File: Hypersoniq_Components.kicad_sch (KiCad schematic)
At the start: 33 parts, among them J1 Conn_01x10_Pin, J2 Conn_01x10_Pin, J3 Conn_01x10_Pin, J4 Eurorack_10_pin_power, U1 TL074, U6 TL072

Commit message: v1.0 Design sent for manufacture
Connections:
- net +12V: now also U6.8 (V+); no longer U6.4 (V-)
- net -12V: now also J3.5 (Pin_5), U6.4 (V-); no longer U6.8 (V+)
- net GND: no longer J3.5 (Pin_5)
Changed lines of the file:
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@@
   (junction (at 35.56 154.94) (diameter 0) (color 0 0 0 0)
   )
+  (junction (at 265.43 138.43) (diameter 0) (color 0 0 0 0)
+  )
   (junction (at 62.23 101.6) (diameter 1.016) (color 0 0 0 0)
   )
@@
   )
   (wire (pts (xy 58.42 171.45) (xy 58.42 172.72))
+    (stroke (width 0) (type default))
+  )
+  (wire (pts (xy 265.43 138.43) (xy 265.43 140.97))
     (stroke (width 0) (type default))
   )
@@
         (path "/5bf2ff82-d6ae-4b65-8172-8e3e49f5daf5"
           (reference "D2") (unit 1)
+        )
+      )
+    )
+  )
+  (symbol (lib_id "power:-12V") (at 265.43 133.35 270) (unit 1)
+    (in_bom yes) (on_board yes) (dnp no)
+    (property "Reference" "#PWR09" (at 267.97 133.35 0)
+      (effects (font (size 1.27 1.27)) hide)
+    )
+    (property "Value" "-12V" (at 267.97 132.08 90)
+      (effects (font (size 1.27 1.27)) (justify left))
+    )
+    (property "Footprint" "" (at 265.43 133.35 0)
+      (effects (font (size 1.27 1.27)) hide)
+    )
+    (property "Datasheet" "" (at 265.43 133.35 0)
+      (effects (font (size 1.27 1.27)) hide)
+    )
+    (pin "1")
+    (instances
+      (project "Hypersoniq_Components"
+        (path "/3008c47a-0b70-48ce-87af-10c40a725fcd"
+          (reference "#PWR09") (unit 1)
+        )
+      )
+      (project "Quilter_Components"
+        (path "/5bf2ff82-d6ae-4b65-8172-8e3e49f5daf5"
+          (reference "#PWR04") (unit 1)
         )
       )
@@
     )
   )
-  (symbol (lib_id "power:GND") (at 265.43 133.35 90) (unit 1)
-    (in_bom yes) (on_board yes) (dnp no)
-    (property "Reference" "#PWR09" (at 271.78 133.35 0)
-      (effects (font (size 1.27 1.27)) hide)
-    )
-    (property "Value" "GND" (at 268.605 132.715 90)
-      (effects (font (size 1.27 1.27)) (justify right))
-    )
-    (property "Footprint" "" (at 265.43 133.35 0)
-      (effects (font (size 1.27 1.27)) hide)
-    )
-    (property "Datasheet" "" (at 265.43 133.35 0)
-      (effects (font (size 1.27 1.27)) hide)
-    )
-    (pin "1")
-    (instances
-      (project "Hypersoniq_Components"
-        (path "/3008c47a-0b70-48ce-87af-10c40a725fcd"
-          (reference "#PWR09") (unit 1)
-        )
-      )
-      (project "Quilter_Components"
-        (path "/5bf2ff82-d6ae-4b65-8172-8e3e49f5daf5"
-          (reference "#PWR0112") (unit 1)
-        )
-      )
-    )
-  )
   (symbol (lib_id "power:GND") (at 143.51 152.4 270) (unit 1)
     (in_bom yes) (on_board yes) (dnp no)
@@
       (effects (font (size 1.27 1.27)) hide)
     )
-    (property "Value" "GND" (at 268.605 137.795 90)
+    (property "Value" "GND" (at 269.24 138.43 90)
       (effects (font (size 1.27 1.27)) (justify right))
     )
@@
     )
   )
-  (symbol (lib_id "Amplifier_Operational:TL072") (at 106.68 161.29 0) (mirror x) (unit 3)
-    (in_bom yes) (on_board yes) (dnp no)
-    (property "Reference" "U6" (at 109.22 160.02 0)
+  (symbol (lib_id "Amplifier_Operational:TL072") (at 101.6 161.29 0) (mirror y) (unit 3)
+    (in_bom yes) (on_board yes) (dnp no) (fields_autoplaced)
+    (property "Reference" "U6" (at 105.41 160.02 0)
       (effects (font (size 1.27 1.27)) (justify right))
     )
-    (property "Value" "TL072" (at 111.76 162.56 0)
+    (property "Value" "TL072" (at 105.41 162.56 0)
       (effects (font (size 1.27 1.27)) (justify right))
     )
-    (property "Footprint" "Package_SO:SO-8_3.9x4.9mm_P1.27mm" (at 106.68 161.29 0)
-      (effects (font (size 1.27 1.27)) hide)
-    )
-    (property "Datasheet" "http://www.ti.com/lit/ds/symlink/tl071.pdf" (at 106.68 161.29 0)
+    (property "Footprint" "Package_SO:SO-8_3.9x4.9mm_P1.27mm" (at 101.6 161.29 0)
+      (effects (font (size 1.27 1.27)) hide)
+    )
+    (property "Datasheet" "http://www.ti.com/lit/ds/symlink/tl071.pdf" (at 101.6 161.29 0)
       (effects (font (size 1.27 1.27)) hide)
     )
@@
         )
       )
-    )
-  )
-  (symbol (lib_id "power:GND") (at 265.43 140.97 90) (unit 1)
-    (in_bom yes) (on_board yes) (dnp no)
-    (property "Reference" "#PWR052" (at 271.78 140.97 0)
-      (effects (font (size 1.27 1.27)) hide)
-    )
-    (property "Value" "GND" (at 268.605 140.335 90)
-      (effects (font (size 1.27 1.27)) (justify right))
-    )
-    (property "Footprint" "" (at 265.43 140.97 0)
-      (effects (font (size 1.27 1.27)) hide)
-    )
-    (property "Datasheet" "" (at 265.43 140.97 0)
-      (effects (font (size 1.27 1.27)) hide)
-    )
-    (pin "1")
-    (instances
-      (project "Hypersoniq_Components"
-        (path "/3008c47a-0b70-48ce-87af-10c40a725fcd"
-          (reference "#PWR052") (unit 1)
-        )
-      )
-      (project "Quilter_Components"
-        (path "/5bf2ff82-d6ae-4b65-8172-8e3e49f5daf5"
-          (reference "#PWR0113") (unit 1)
-        )
-      )

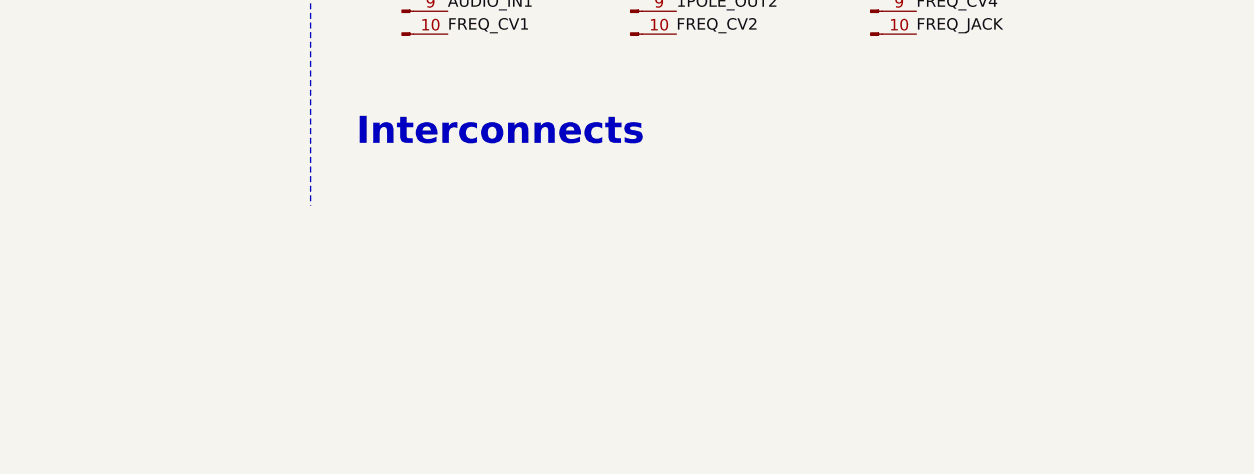
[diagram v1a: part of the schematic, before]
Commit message: Added v1.0 component schematic pdf
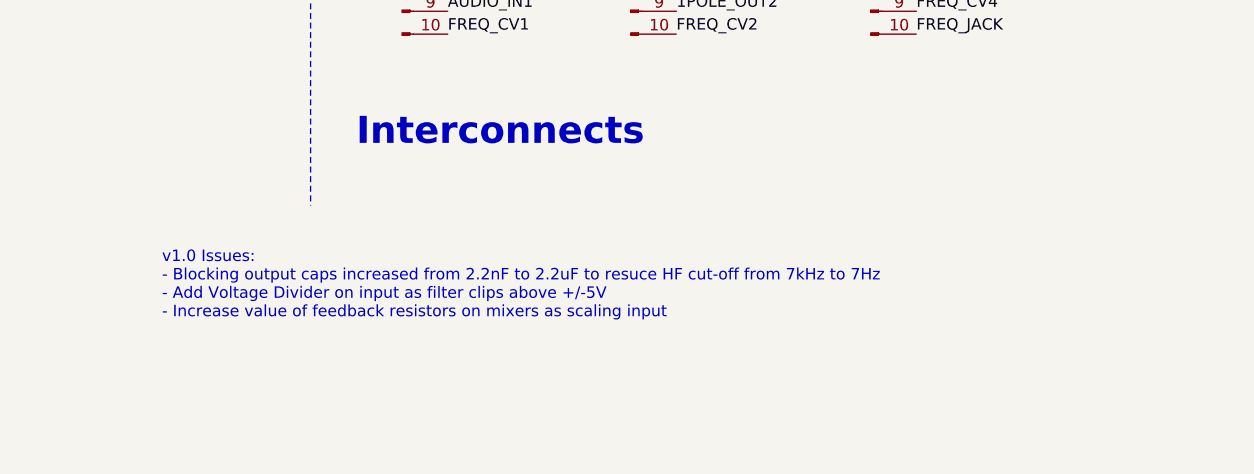
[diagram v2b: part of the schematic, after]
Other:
- note added: "v1.0 Issues: - Blocking output caps increased from 2.2nF to 2.2uF to resuce HF cut-off from 7kHz to 7Hz - Add Voltage Divider on input as filter clips above +/-5V - Increase value of feedback resistors on mixers as scaling input"
- company: (none) -> Mountjoy Modular
- title: (none) -> Hypersoniq
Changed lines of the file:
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@@
 (kicad_sch (version 20230121) (generator eeschema)
   (paper "A4")
+  (title_block
+    (title "Hypersoniq")
+    (date "2023-08-12")
+    (rev "1.0")
+    (company "Mountjoy Modular")
+  )
   (junction (at 35.56 165.1) (diameter 0) (color 0 0 0 0)
   )
@@
     (effects (font (size 1.27 1.27)) (justify left bottom))
   )
+  (text "v1.0 Issues:\n- Blocking output caps increased from 2.2nF to 2.2uF to resuce HF cut-off from 7kHz to 7Hz\n- Add Voltage Divider on input as filter clips above +/-5V\n- Increase value of feedback resistors on mixers as scaling input"
+    (at 181.61 177.8 0)
+    (effects (font (size 1.27 1.27)) (justify left bottom))
+  )

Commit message: Minor changes
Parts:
- R64, R70: value 4.7k -> 6.8k
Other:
- note added: "Gain: -6.8k / 10k = -0.68"
- note removed: "Gain: -4.7k / 10k = -0.47"
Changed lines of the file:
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@@
     (title "Hypersoniq")
     (date "2023-08-12")
-    (rev "1.0")
+    (rev "2.0")
     (company "Mountjoy Modular")
   )
@@
     (effects (font (size 3 3) (thickness 0.6) bold) (justify left bottom))
   )
-  (text "Gain: -4.7k / 10k = -0.47\n " (at 160.02 113.03 0)
-    (effects (font (size 1.27 1.27)) (justify left bottom))
-  )
-  (text "Gain: -4.7k / 10k = -0.47\n " (at 68.58 113.03 0)
+  (text "Gain: -6.8k / 10k = -0.68\n " (at 91.44 125.73 0)
     (effects (font (size 1.27 1.27)) (justify left bottom))
   )
@@
       (effects (font (size 0.889 0.889)))
     )
-    (property "Value" "4.7k" (at 144.78 88.9 90)
+    (property "Value" "6.8k" (at 144.78 88.9 90)
       (effects (font (size 1.27 1.27)))
     )
@@
       (effects (font (size 0.889 0.889)))
     )
-    (property "Value" "4.7k" (at 53.34 88.9 90)
-      (effects (font (size 1.27 1.27)))
-    )
+    (property "Value" "6.8k" (at 53.34 88.9 90)
+      (effects (font (size 1.27 1.27)))
+    )
